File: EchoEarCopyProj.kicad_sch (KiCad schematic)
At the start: 0 parts

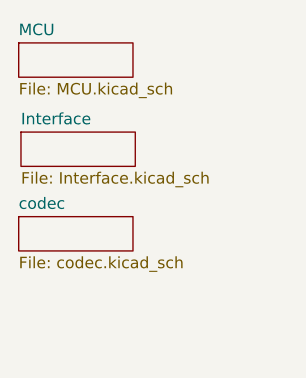
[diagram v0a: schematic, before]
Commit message: done schematic without all footprints
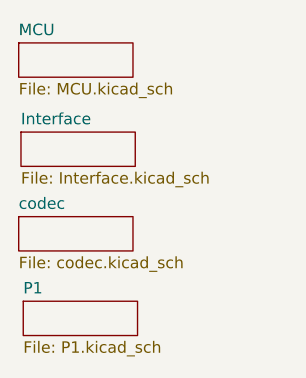
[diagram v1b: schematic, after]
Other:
- added sheet P1 (P1.kicad_sch)
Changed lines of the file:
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@@
+	)
+	(sheet
+		(at 13.208 43.434)
+		(size 12.7 3.81)
+		(exclude_from_sim no)
+		(in_bom yes)
+		(on_board yes)
+		(dnp no)
+		(fields_autoplaced yes)
+		(stroke
+			(width 0.1524)
+			(type solid)
+		)
+		(fill
+			(color 0 0 0 0.0000)
+		)
+		(property "Sheetname" "P1"
+			(at 13.208 42.7224 0)
+			(effects
+				(font
+					(size 1.27 1.27)
+				)
+				(justify left bottom)
+			)
+		)
+		(property "Sheetfile" "P1.kicad_sch"
+			(at 13.208 47.8286 0)
+			(effects
+				(font
+					(size 1.27 1.27)
+				)
+				(justify left top)
+			)
+		)
+		(instances
+			(project "EchoEarCopyProj"
+				(path "/cbd96126-2c6b-41c3-991f-657fa8ab5ecf"
+					(page "5")
+				)
+			)
+		)
 	)
 	(sheet
